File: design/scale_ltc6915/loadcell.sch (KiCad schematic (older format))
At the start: 24 parts, among them J3 Load cell, U4 LTC6915, U5 LM2703, U6 LP2985-5.0, U7 ADS8320E_2K5, U8 LM4140CCM-2.5

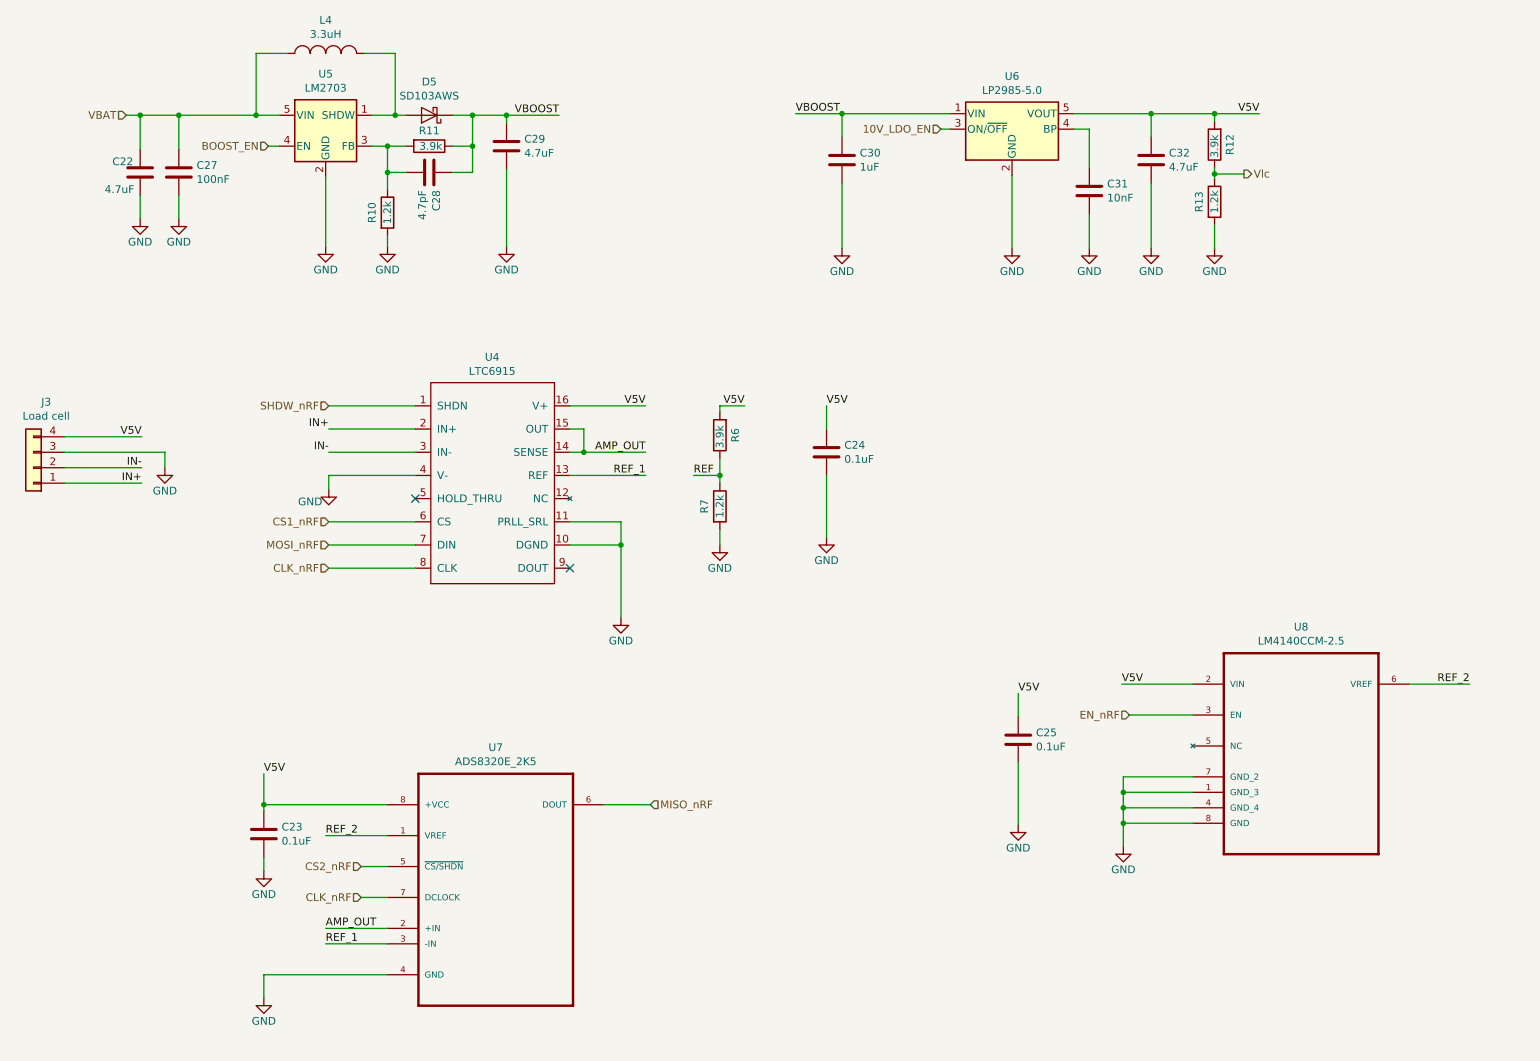
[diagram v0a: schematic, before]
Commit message: updated schematic of scale_ltc6915, fixed issues
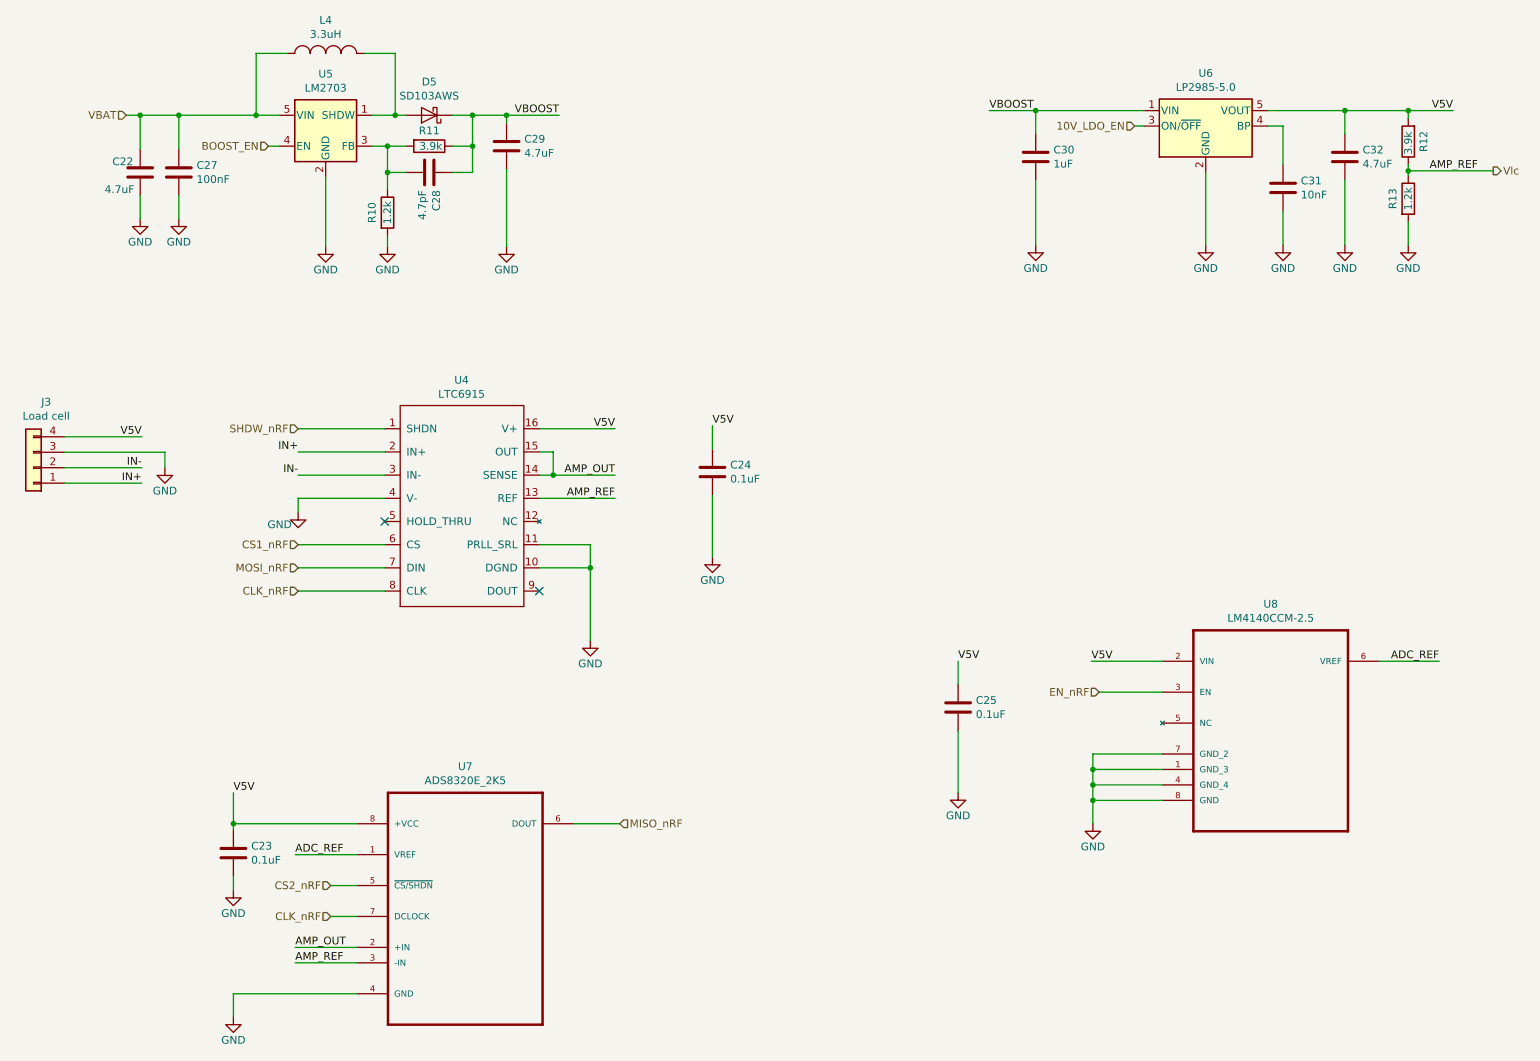
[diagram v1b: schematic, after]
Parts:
- removed R6: 3.9k, Resistor_SMD:R_0603_1608Metric_Pad1.05x0.95mm_HandSolder, symbol sense:R
- removed R7: 1.2k, Resistor_SMD:R_0603_1608Metric_Pad1.05x0.95mm_HandSolder, symbol sense:R
- U4: footprint (none) -> Package_SO:SSOP-16_3.9x4.9mm_P0.635mm
- U7: footprint SOP65P490X110-8N -> Package_SO:VSSOP-8_3.0x3.0mm_P0.65mm
- U8: footprint SOIC127P600X175-8N -> Package_SO:SOIC-8_3.9x4.9mm_P1.27mm
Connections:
- net REF_1 is gone; now on net Vlc: U4.13 (REF), U7.3 (-IN)
- net REF_2 renamed ADC_REF
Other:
- moved on the sheet: C23, C24, C25, C30, C31, C32, R12, R13, U4, U6, U7, U8

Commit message: BOMs, schematics updated, scale_ltc6915 PCB Design complete.
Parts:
- renumbered C27 to C26, C28 to C27, C29 to C28, C30 to C29, C31 to C30, C32 to C31, R10 to R6, R11 to R7, R12 to R8, R13 to R9
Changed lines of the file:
@@
 $EndComp
 $Comp
-L sense:R R11
+L sense:R R7
 U 1 1 5E6E38F6
 P 3370 1440
-F 0 "R11" V 3270 1440 50  0000 C CNN
+F 0 "R7" V 3270 1440 50  0000 C CNN
 F 1 "3.9k" V 3370 1450 50  0000 C CNN
 F 2 "Resistor_SMD:R_0603_1608Metric_Pad1.05x0.95mm_HandSolder" V 3300 1440 50  0001 C CNN
@@
 $EndComp
 $Comp
-L sense:R R10
+L sense:R R6
 U 1 1 5E6E4142
 P 3100 1870
-F 0 "R10" V 3000 1870 50  0000 C CNN
+F 0 "R6" V 3000 1870 50  0000 C CNN
 F 1 "1.2k" V 3100 1870 50  0000 C CNN
 F 2 "Resistor_SMD:R_0603_1608Metric_Pad1.05x0.95mm_HandSolder" V 3030 1870 50  0001 C CNN
@@
 $EndComp
 $Comp
-L Device:C C27
+L Device:C C26
 U 1 1 5E6E440E
 P 1750 1610
-F 0 "C27" H 1865 1656 50  0000 L CNN
+F 0 "C26" H 1865 1656 50  0000 L CNN
 F 1 "100nF" H 1865 1565 50  0000 L CNN
 F 2 "Capacitor_SMD:C_0603_1608Metric_Pad1.05x0.95mm_HandSolder" H 1788 1460 50  0001 C CNN
@@
 $EndComp
 $Comp
-L Device:C C28
+L Device:C C27
 U 1 1 5E6E4653
 P 3370 1610
-F 0 "C28" H 3485 1656 50  0000 L CNN
+F 0 "C27" H 3485 1656 50  0000 L CNN
 F 1 "4.7pF" H 3485 1565 50  0000 L CNN
 F 2 "Capacitor_SMD:C_0603_1608Metric_Pad1.05x0.95mm_HandSolder" H 3408 1460 50  0001 C CNN
@@
 $EndComp
 $Comp
-L Device:C C29
+L Device:C C28
 U 1 1 5E6E4B7F
 P 3870 1440
-F 0 "C29" H 3985 1486 50  0000 L CNN
+F 0 "C28" H 3985 1486 50  0000 L CNN
 F 1 "4.7uF" H 3985 1395 50  0000 L CNN
 F 2 "Capacitor_SMD:C_0603_1608Metric_Pad1.05x0.95mm_HandSolder" H 3908 1290 50  0001 C CNN
@@
 $EndComp
 $Comp
-L Device:C C30
+L Device:C C29
 U 1 1 5E6EF6C5
 P 7293 1510
-F 0 "C30" H 7408 1556 50  0000 L CNN
+F 0 "C29" H 7408 1556 50  0000 L CNN
 F 1 "1uF" H 7408 1465 50  0000 L CNN
 F 2 "Capacitor_SMD:C_0603_1608Metric_Pad1.05x0.95mm_HandSolder" H 7331 1360 50  0001 C CNN
@@
 $EndComp
 $Comp
-L Device:C C31
+L Device:C C30
 U 1 1 5E6EF9CE
 P 8893 1710
-F 0 "C31" H 9008 1756 50  0000 L CNN
+F 0 "C30" H 9008 1756 50  0000 L CNN
 F 1 "10nF" H 9008 1665 50  0000 L CNN
 F 2 "Capacitor_SMD:C_0603_1608Metric_Pad1.05x0.95mm_HandSolder" H 8931 1560 50  0001 C CNN
@@
 $EndComp
 $Comp
-L Device:C C32
+L Device:C C31
 U 1 1 5E6F04D3
 P 9293 1510
-F 0 "C32" H 9408 1556 50  0000 L CNN
+F 0 "C31" H 9408 1556 50  0000 L CNN
 F 1 "4.7uF" H 9408 1465 50  0000 L CNN
 F 2 "Capacitor_SMD:C_0603_1608Metric_Pad1.05x0.95mm_HandSolder" H 9331 1360 50  0001 C CNN
@@
 	8893 1310 8893 1560
 $Comp
-L sense:R R13
+L sense:R R9
 U 1 1 5E7E7C0C
 P 9703 1780
-F 0 "R13" V 9603 1780 50  0000 C CNN
+F 0 "R9" V 9603 1780 50  0000 C CNN
 F 1 "1.2k" V 9703 1780 50  0000 C CNN
 F 2 "Resistor_SMD:R_0603_1608Metric_Pad1.05x0.95mm_HandSolder" V 9633 1780 50  0001 C CNN
@@
 $EndComp
 $Comp
-L sense:R R12
+L sense:R R8
 U 1 1 5E7E7EA2
 P 9703 1410
-F 0 "R12" V 9603 1410 50  0000 C CNN
+F 0 "R8" V 9603 1410 50  0000 C CNN
 F 1 "3.9k" V 9703 1420 50  0000 C CNN
 F 2 "Resistor_SMD:R_0603_1608Metric_Pad1.05x0.95mm_HandSolder" V 9633 1410 50  0001 C CNN
